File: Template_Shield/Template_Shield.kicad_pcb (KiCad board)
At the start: 2 copper layers, 68.6 x 53.3 mm, 99 parts, among them IC1 CAT811TTBI-CT3, IC10 SN74LVC1G125DCKR, IC2 NX1117CE33Z, IC4 SN74LVC1G125DCKR, IC6 0982_W5500, IC8 SN74LVC1G125DCKR, IC9 SN74LVC1G125DCKR, Q2 25MHz KX-7_NM, T2 PMV48XP, X1 0046_15TW-882

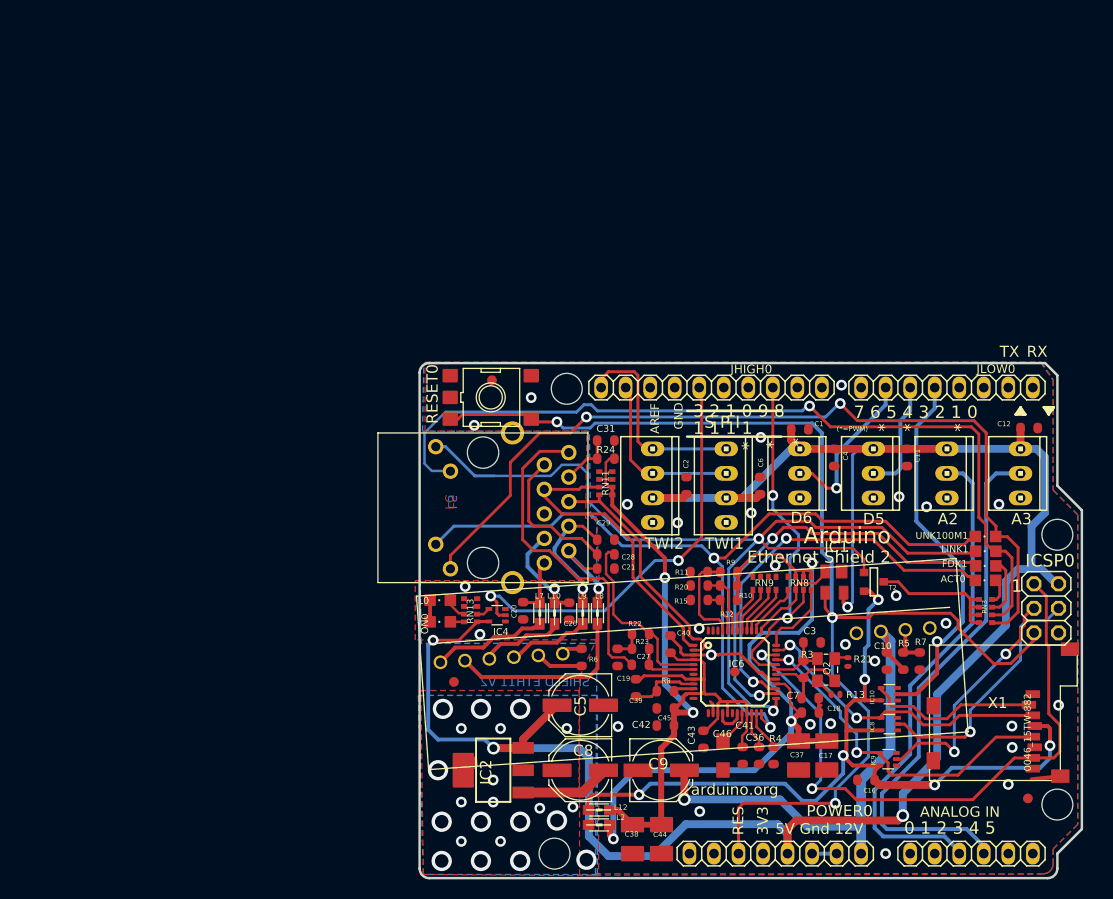
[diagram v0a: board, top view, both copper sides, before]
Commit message: added datasheet and header models to PCB
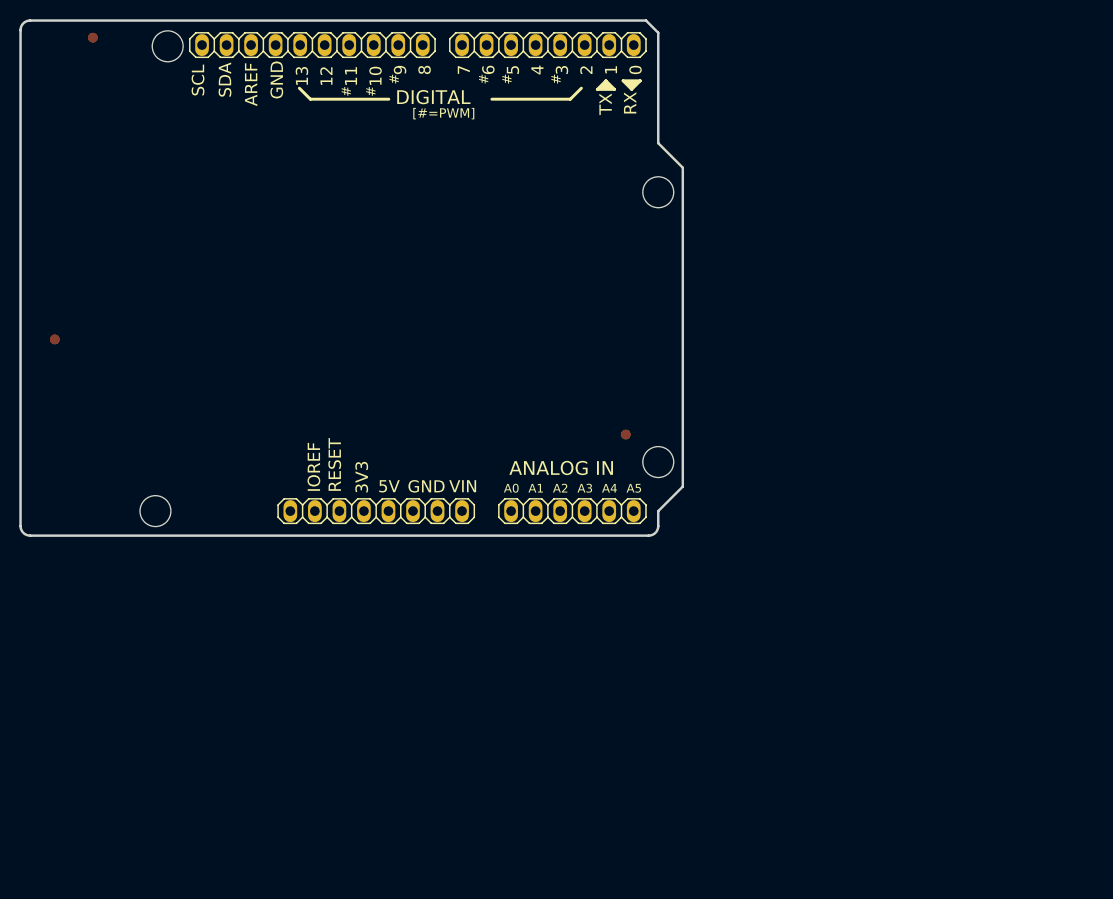
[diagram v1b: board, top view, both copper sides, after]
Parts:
- removed A2, A3: white IN, Arduino-Ethernet-Shield2-V2:10X03MTA
- removed ACT0, L0, ON0, UNK100M1: Green, Arduino-Ethernet-Shield2-V2:CHIPLED_0805
- removed C1, C11, C12, C18, C2, C31, C39, C4, C40, C41, C42, C43, C45, C6: 100n, Arduino-Ethernet-Shield2-V2:C0603-ROUND
- removed C10, C16: 1uF, Arduino-Ethernet-Shield2-V2:C0603-ROUND
- removed C17, C37, C38, C44: 22uF, Arduino-Ethernet-Shield2-V2:SMC_B
- removed C19, C20, C21, C26, C29, C36: 10n, Arduino-Ethernet-Shield2-V2:C0603-ROUND
- removed C27, C28: 10nF, Arduino-Ethernet-Shield2-V2:C0603-ROUND
- removed C3, C7: 10p, Arduino-Ethernet-Shield2-V2:C0603-ROUND
- removed C46: 4u7, Arduino-Ethernet-Shield2-V2:SMC_A
- removed C5, C8, C9: 47u, Arduino-Ethernet-Shield2-V2:PANASONIC_D
- removed D5, D6: orange OUT, Arduino-Ethernet-Shield2-V2:10X03MTA
- removed FDX1, LINK1: Yellow, Arduino-Ethernet-Shield2-V2:CHIPLED_0805
- removed IC1: CAT811TTBI-CT3, Arduino-Ethernet-Shield2-V2:SOT143
- removed IC10, IC4, IC8, IC9: SN74LVC1G125DCKR, Arduino-Ethernet-Shield2-V2:SC70-5
- removed IC2: NX1117CE33Z, Arduino-Ethernet-Shield2-V2:SOT223
- removed IC6: 0982_W5500, Arduino-Ethernet-Shield2-V2:TQFP48-7X7
- removed ICSP0: 3x2F-H11, Arduino-Ethernet-Shield2-V2:2X03
- removed L10, L12, L2, L7, L8, L9: MH2029-300Y, Arduino-Ethernet-Shield2-V2:0805
- removed Q2: 25MHz KX-7_NM, Arduino-Ethernet-Shield2-V2:CRYSTAL3.2X2.5
- removed R10, R11, R12, R15, R20, R22, R23, R9: 10k, Arduino-Ethernet-Shield2-V2:R0603-ROUND
- removed R13, R21: 0R, Arduino-Ethernet-Shield2-V2:R0402
- removed R24: 22R, Arduino-Ethernet-Shield2-V2:R0603-ROUND
- removed R3: 1M, Arduino-Ethernet-Shield2-V2:R0603-ROUND
- removed R4: 10K, Arduino-Ethernet-Shield2-V2:R0603-ROUND
- removed R5, R6, R7: 0R, Arduino-Ethernet-Shield2-V2:R0603-ROUND
- removed R8: 12k4_1%, Arduino-Ethernet-Shield2-V2:R0603-ROUND
- removed RESET0: , Arduino-Ethernet-Shield2-V2:TS42
- removed RN11: 49R9, Arduino-Ethernet-Shield2-V2:CAY16
- removed RN13: 1k, Arduino-Ethernet-Shield2-V2:CAY16
- removed RN3: 470R, Arduino-Ethernet-Shield2-V2:CAY16
- removed RN8, RN9: 10k, Arduino-Ethernet-Shield2-V2:CAY16
- removed T2: PMV48XP, Arduino-Ethernet-Shield2-V2:SOT-23
- removed TWI1, TWI2: Verde TWI, Arduino-Ethernet-Shield2-V2:10X04MTA
- removed UC1: RB1-125BHQ1A, Arduino-Ethernet-Shield2-V2:POE-RJ45
- removed X1: 0046_15TW-882, Arduino-Ethernet-Shield2-V2:SDCARD-15TW-8821
- removed ZZ1: AG9612-2BR, Arduino-Ethernet-Shield2-V2:AG9000
- AD0: renamed from JANALOG0; value FH254-106DF085149V_PRESSFIT -> SSQ-106-04-F-S; footprint Arduino-Ethernet-Shield2-V2:1X06-TH-PRESSFIT -> arduino_shield:1X06-TH-PRESSFIT
- IOH0: renamed from JHIGH0; value FH254-110DF085149V_PRESSFIT -> SSQ-110-04-F-S; footprint Arduino-Ethernet-Shield2-V2:1X10-TH-PRESSFIT -> arduino_shield:1X10-TH-PRESSFIT
- IOL0: renamed from JLOW0; value FH254-108DF085149V_PRESSFIT -> SSQ-108-04-F-S; footprint Arduino-Ethernet-Shield2-V2:1X08-TH-PRESSFIT -> arduino_shield:1X08-TH-PRESSFIT
- POWER0: value FH254-108DF085149V_PRESSFIT -> SSQ-108-04-F-S; footprint Arduino-Ethernet-Shield2-V2:1X08-TH-PRESSFIT -> arduino_shield:1X08-TH-PRESSFIT
- moved FID2 56.2 mm to (133.7, 74.5)
- moved UNK_HOLE_0 54.5 mm to (137.0, 49.4)
- moved UNK_HOLE_1 54.5 mm to (137.0, 77.4)
- moved AD0 54.5 mm to (128.2, 82.5), turned to 180 degrees
- moved FID3 54.5 mm to (78.5, 33.4)
- moved FID4 54.5 mm to (74.6, 64.7)
- moved IOH0 54.5 mm to (101.2, 34.2)
- moved IOL0 54.5 mm to (125.6, 34.2)
- moved POWER0 54.5 mm to (107.8, 82.5), turned to 180 degrees
- moved UNK_HOLE_2 54.5 mm to (86.2, 34.3)
- moved UNK_HOLE_3 54.5 mm to (85.0, 82.5)
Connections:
- net AREF renamed /AREF
- net PD0 renamed /D0/RX
- net PD1 renamed /D1/TX
- net PD2 renamed /D2
- net PD3 renamed /D3~
- AD0 pad 1: (no net) -> /A5
- AD0 pad 2: (no net) -> /A4
- AD0 pad 3: A2 -> /A3
- AD0 pad 4: A3 -> /A2
- AD0 pad 5: (no net) -> /A1
- AD0 pad 6: (no net) -> /A0
- IOH0 pad 1: (no net) -> /D8
- IOH0 pad 10: SCL -> /D19/SCL
- IOH0 pad 2: (no net) -> /D9~
- IOH0 pad 3: IO10*/SS -> /D10~
- IOH0 pad 4: (no net) -> /D11~
- IOH0 pad 5: (no net) -> /D12
- IOH0 pad 6: IO13* -> /D13
- IOH0 pad 7: GND -> /GND
- IOH0 pad 9: SDA -> /D18/SDA
- IOL0 pad 5: D4/SD_CS -> /D4
- IOL0 pad 6: D5 -> /D5~
- IOL0 pad 7: D6 -> /D6~
- IOL0 pad 8: (no net) -> /D7
- POWER0 pad 1: (no net) -> /VIN
- POWER0 pad 2: (no net) -> /GND
- POWER0 pad 3: RESET -> /GND
- POWER0 pad 4: (no net) -> /+5V
- POWER0 pad 5: +5V -> /+3V3
- POWER0 pad 6: GND -> /RESET
- POWER0 pad 7: GND -> /IOREF
- POWER0 pad 8: VIN -> unconnected-(POWER0-Pin_8-Pad8)
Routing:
- net +5V: track 214.0 -> 0.00 mm, vias 4 -> 0
- net RESET: track 124.8 -> 0.00 mm, vias 3 -> 0
- net LINKLED: track 101.7 -> 0.00 mm, vias 2 -> 0
- net N$25: track 90.5 -> 0.00 mm, vias 2 -> 0
- net +3V3: track 89.4 -> 0.00 mm, vias 28 -> 0
- net N$22: track 88.9 -> 0.00 mm, vias 1 -> 0
- net SPDLED: track 85.6 -> 0.00 mm, vias 2 -> 0
- net +3V3A: track 84.8 -> 0.00 mm, vias 2 -> 0
- net +3V3D: track 80.0 -> 0.00 mm, vias 3 -> 0
- net MISO: track 64.9 -> 0.00 mm, vias 2 -> 0
- net A3: track 56.0 -> 0.00 mm
- net A2: track 53.0 -> 0.00 mm
- net VIN: track 52.2 -> 0.00 mm, vias 1 -> 0
- net GND: track 46.9 -> 0.00 mm, vias 28 -> 0
- net FDXLED: track 44.5 -> 0.00 mm, vias 2 -> 0
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- removed copper zone on B.Cu, net +3V3
- removed copper zone on F.Cu, net +3V3
- removed copper zone on B.Cu, net GND
- removed copper zone on F.Cu, net GND
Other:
- board text added: "#"
- board text added: "0"
- board text added: "10"
- board text added: "11"
- board text added: "12"
- board text added: "13"
- board text added: "2"
- board text added: "3"
- board text added: "4"
- board text added: "5"
- board text added: "5V"
- board text added: "6"
- board text added: "7"
- board text added: "8"
- board text added: "9"
- board text added: "A0"
- board text added: "A1"
- board text added: "A2"
- board text added: "A3"
- board text added: "A4"
- board text added: "A5"
- board text added: "DIGITAL"
- board text added: "IOREF"
- board text added: "RESET"
- board text added: "SCL"
- board text added: "SDA"
- board text added: "VIN"
- board text added: "[#=PWM]"
- board text removed: "(*=PWM)"
- board text removed: "*"
- board text removed: "0 1 2 3 4 5"
- board text removed: "1 1 1 1"
- board text removed: "3 2 1 0 9 8"
- board text removed: "5V Gnd 12V"
- board text removed: "7 6 5 4 3 2 1 0"
- board text removed: "Arduino"
- board text removed: "Ethernet Shield 2"
- board text removed: "LC"
- board text removed: "LS"
- board text removed: "RES"
- board text removed: "S P I"
- board text removed: "SHIELD ETH11 V2"
- board text removed: "arduino.org"
